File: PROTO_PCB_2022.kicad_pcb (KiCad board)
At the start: 2 copper layers, 90.8 x 50.2 mm, 35 parts, among them J1 12V_IN, J10 12V_AUX, J11 SW_START, J12 VESC_START, J2 SW_KILL_DRIVER, J3 SW_KILL_LEFT, J4 SW_KILL_RIGHT, J5 12V_ECU, J6 12V_HORN, J7 SW_BRAKE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

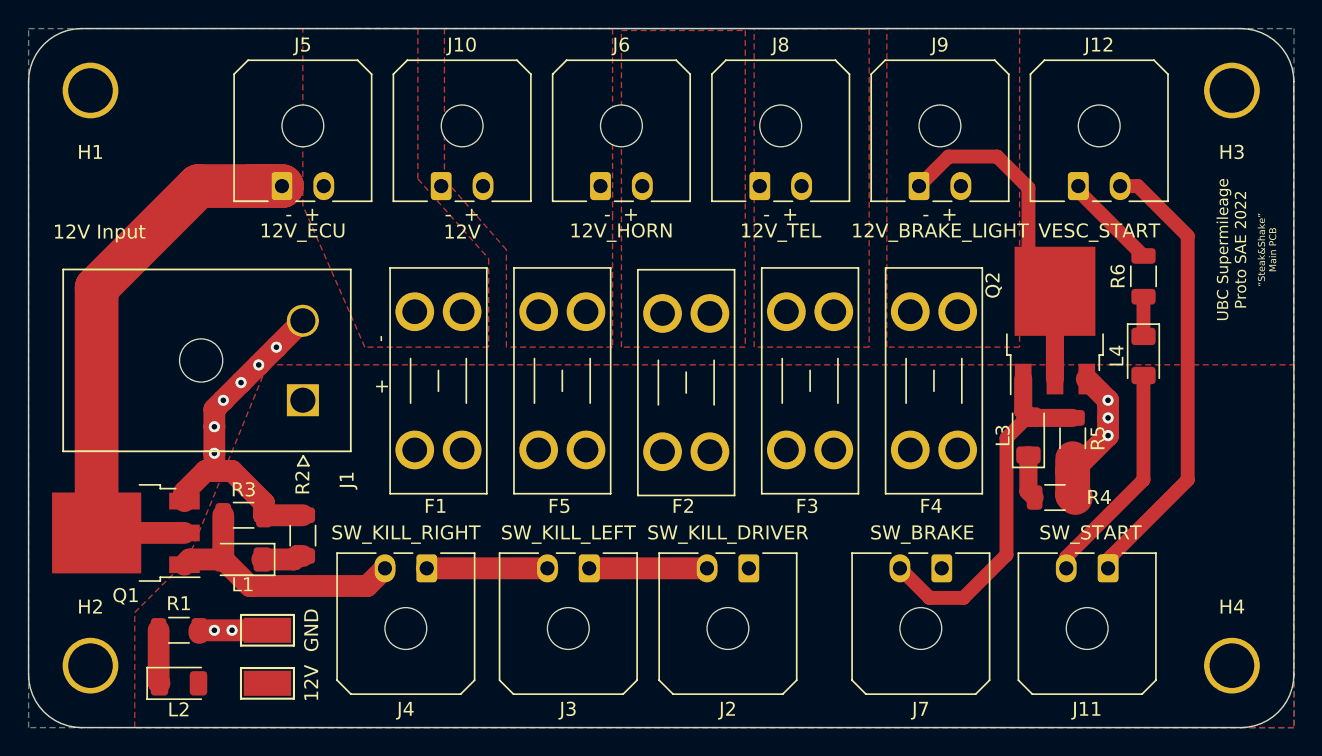
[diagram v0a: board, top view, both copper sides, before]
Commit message: added some more labels to layout and made BOM doc
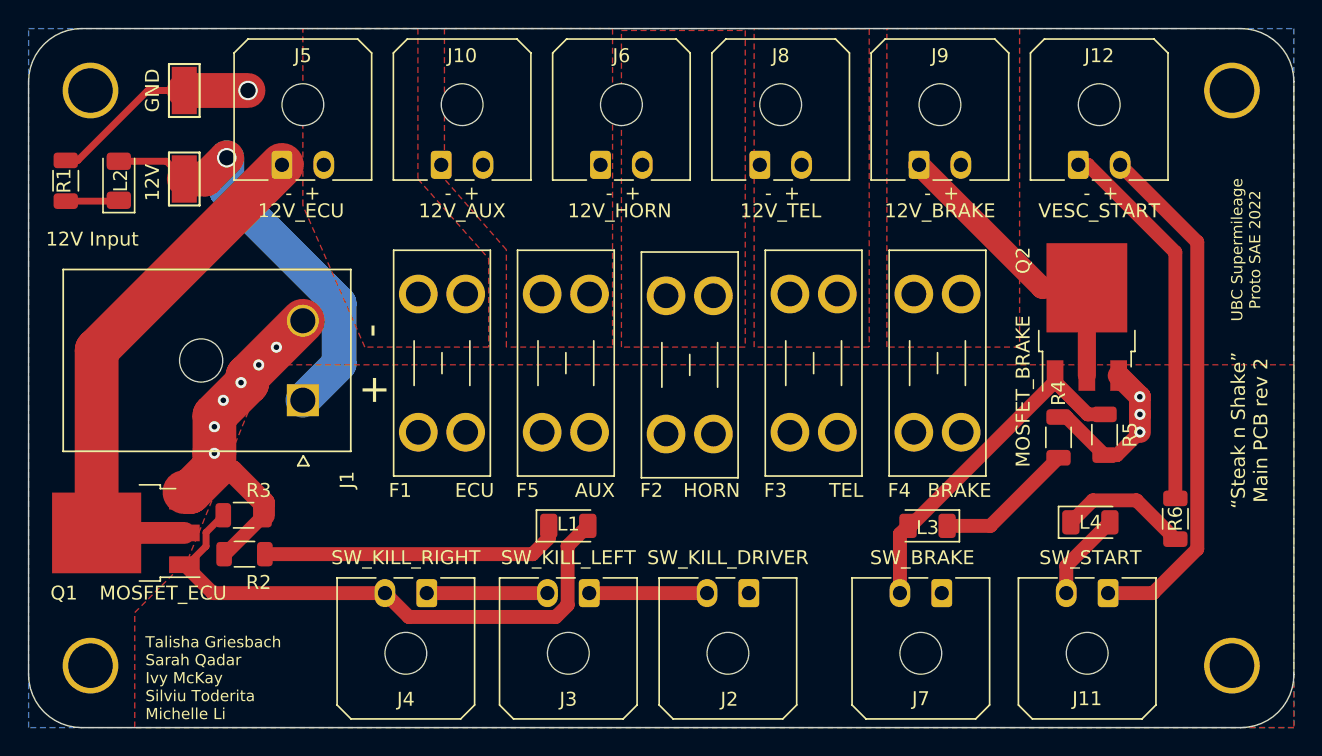
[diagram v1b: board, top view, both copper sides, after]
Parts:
- added ?: , , F.Cu at (121.4, 113.5)
- added ?: , , F.Cu at (122.9, 126.2)
- added ?: , , F.Cu at (121.7, 122.2)
- J9: value 12V_BRAKE_LIGHT -> 12V_BRAKE
- Q2: value MOSFET_BRAKE_LIGHT -> MOSFET_BRAKE
- TP1: value 12V Test -> 12V
- TP2: value GND Test -> GND
- moved TP2 39.2 mm to (52.8, 104.1), turned to 90 degrees
- moved TP1 36.7 mm to (52.8, 110.5), turned to 90 degrees
- moved L2 36.3 mm to (48.1, 110.6), turned to 90 degrees
- moved R1 33.3 mm to (44.3, 110.6), turned to 270 degrees
- moved L1 23.5 mm to (80.4, 135.4), turned to 0 degrees
- moved R6 17.5 mm to (124.0, 134.9)
- moved L4 12.5 mm to (117.9, 135.1), turned to 0 degrees
- moved L3 9.71 mm to (106.2, 135.4), turned to 180 degrees
- moved R2 4.40 mm to (57.1, 137.4), turned to 180 degrees
- moved R4 4.33 mm to (115.6, 129.0), turned to 90 degrees
- moved Q2 2.30 mm to (117.6, 120.4)
- moved R5 2.30 mm to (118.9, 128.8)
- moved J11 1.78 mm to (119.1, 140.2)
- moved J2 1.78 mm to (93.3, 140.2)
- moved J3 1.78 mm to (81.9, 140.2)
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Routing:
- net +12V: track 0.00 -> 30.7 mm, vias 0 -> 1
- net GND: track 42.5 -> 69.1 mm, vias 11 -> 10
- net Net-(J4-Pad2): track 19.0 -> 40.5 mm
- net Net-(J12-Pad1): track 6.61 -> 27.2 mm
- net Net-(L1-Pad1): track 3.02 -> 21.7 mm
- net Net-(J5-Pad1): track 56.8 -> 39.1 mm
- net Net-(J11-Pad2): track 16.1 -> 6.38 mm
- net Net-(L3-Pad1): track 3.23 -> 10.0 mm
- net Net-(L4-Pad1): track 2.85 -> 9.30 mm
- net Net-(J11-Pad1): track 33.6 -> 37.6 mm
- net Net-(J7-Pad2): track 26.5 -> 25.3 mm
- net Net-(J9-Pad1): track 24.2 -> 24.7 mm
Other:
- board text added: "12V_AUX"
- board text added: "AUX"
- board text added: "BRAKE"
- board text added: "ECU"
- board text added: "HORN"
- board text added: "TEL"
- board text added: "Talisha Griesbach Sarah Qadar Ivy McKay Silviu Toderita Michelle Li"
- board text added: "“Steak n Shake” Main PCB rev 2"
- board text removed: "12V"
- board text removed: "GND"
- board text removed: "“Steak&Shake” Main PCB"

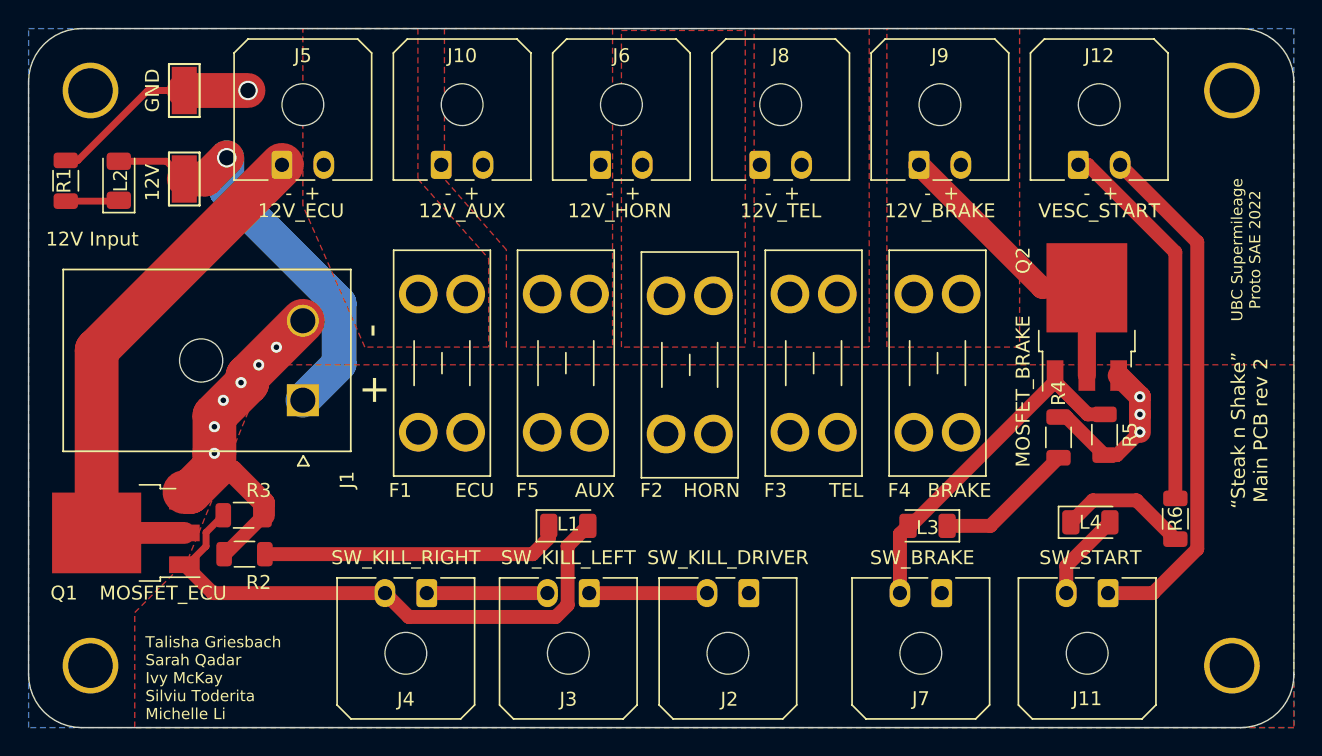
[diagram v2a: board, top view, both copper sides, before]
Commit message: Changes handlebar connector to RJ45
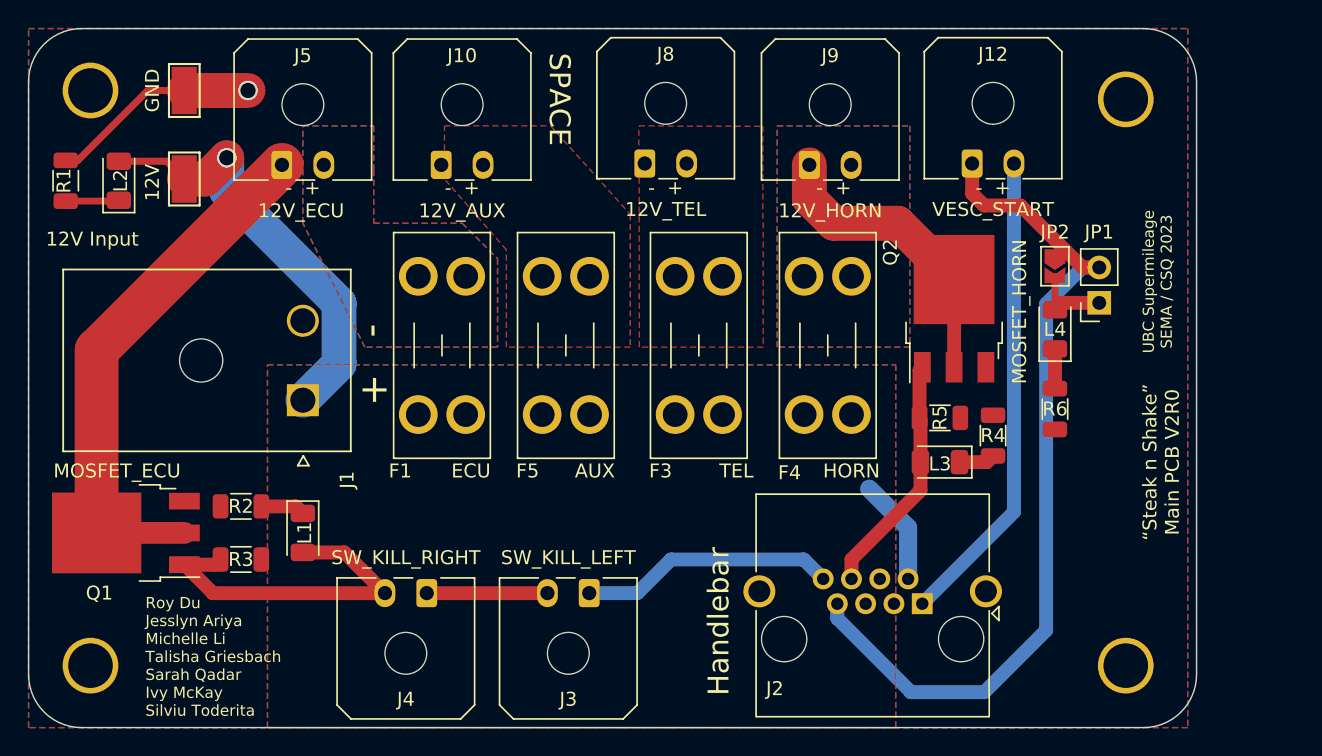
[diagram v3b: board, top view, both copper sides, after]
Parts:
- removed ? (x3): , 
- removed F2: 2A, Fuse:Fuseholder_Blade_Mini_Keystone_3568
- removed J11: SW_START, Connector_Molex:Molex_Micro-Fit_3.0_43650-0200_1x02_P3.00mm_Horizontal
- removed J6: 12V_HORN, Connector_Molex:Molex_Micro-Fit_3.0_43650-0200_1x02_P3.00mm_Horizontal
- removed J7: SW_BRAKE, Connector_Molex:Molex_Micro-Fit_3.0_43650-0200_1x02_P3.00mm_Horizontal
- added JP1: Jumper_2_Open, Connector_PinSocket_2.54mm:PinSocket_1x02_P2.54mm_Vertical, F.Cu at (118.5, 119.4)
- added JP2: SolderJumper_2_Open, Jumper:SolderJumper-2_P1.3mm_Open_TrianglePad1.0x1.5mm, F.Cu at (115.3, 116.8)
- J2: value SW_KILL_DRIVER -> Ethernet connector; footprint Connector_Molex:Molex_Micro-Fit_3.0_43650-0200_1x02_P3.00mm_Horizontal -> Connector_RJ:RJ45_Amphenol_RJHSE5380
- J9: value 12V_BRAKE -> 12V_HORN
- Q2: value MOSFET_BRAKE -> MOSFET_HORN
- moved L1 19.1 mm to (61.3, 135.9), turned to -90 degrees
- moved L4 14.1 mm to (115.3, 121.3), turned to 90 degrees
- moved J2 12.5 mm to (105.8, 141.0)
- moved R5 11.9 mm to (107.1, 127.6), turned to 0 degrees
- moved R6 11.7 mm to (115.3, 127.0)
- moved Q2 9.54 mm to (108.1, 119.8)
- moved F3 8.34 mm to (91.5, 117.5)
- moved J8 8.26 mm to (85.9, 109.4)
- moved F4 7.98 mm to (100.7, 117.5)
- moved J9 7.87 mm to (97.7, 109.5)
- moved H3 7.65 mm to (120.4, 104.8)
- moved J12 7.62 mm to (109.4, 109.4)
- moved H4 7.62 mm to (120.4, 145.4)
- moved R4 4.70 mm to (110.9, 128.9)
- moved L3 4.66 mm to (107.1, 130.8)
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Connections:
- J12 pad 1: Net-(J12-Pad1) -> /Starter_in
- J12 pad 2: Net-(J11-Pad1) -> /Starter_out
- J2 pad 1: +12V -> /Starter_out
- J2 pad 2: Net-(J2-Pad2) -> +12V
- J3 pad 1: Net-(J2-Pad2) -> /Kill
- L3 pad 2: Net-(J7-Pad2) -> /Horn
- Q2 pad 1: Net-(J7-Pad2) -> /Horn
- R5 pad 1: Net-(J7-Pad2) -> /Horn
- R6 pad 1: Net-(L4-Pad1) -> GND
- R6 pad 2: Net-(J12-Pad1) -> Net-(L4-Pad1)
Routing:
- net /Starter_in: track 0.00 -> 61.9 mm
- net GND: track 69.1 -> 15.2 mm, vias 10 -> 1
- net Net-(J11-Pad1): track 37.6 -> 0.00 mm
- net /Starter_out: track 0.00 -> 34.3 mm
- net Net-(J12-Pad1): track 27.2 -> 0.00 mm
- net Net-(J7-Pad2): track 25.3 -> 0.00 mm
- net Net-(L1-Pad1): track 21.7 -> 3.19 mm
- net /Kill: track 0.00 -> 18.4 mm
- net /Horn: track 0.00 -> 17.3 mm
- net Net-(J4-Pad2): track 40.5 -> 25.1 mm
- net Net-(J2-Pad2): track 8.45 -> 0.00 mm
- net +12V: track 30.7 -> 38.4 mm
- net Net-(L3-Pad1): track 10.0 -> 2.59 mm
- net Net-(L4-Pad1): track 9.30 -> 2.85 mm
- net Net-(J9-Pad1): track 24.7 -> 22.6 mm
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- added copper zone on B.Cu, net +12V
- added copper zone on F.Cu, net GND
- added copper zone on B.Cu, net Net-(F1-Pad1)
- added copper zone on B.Cu, net Net-(F4-Pad1)
- removed copper zone on F.Cu, net Net-(F2-Pad1)
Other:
- board size 90.8 x 50.2 mm -> 83.8 x 50.2 mm
- net class Default removed
- board text added: "Handlebar"
- board text added: "Roy Du Jesslyn Ariya Michelle Li Talisha Griesbach Sarah Qadar Ivy McKay Silviu Toderita"
- board text added: "SPACE"
- board text added: "UBC Supermileage SEMA / CSQ 2023"
- board text added: "“Steak n Shake” Main PCB V2R0"
- board text removed: "BRAKE"
- board text removed: "Talisha Griesbach Sarah Qadar Ivy McKay Silviu Toderita Michelle Li"
- board text removed: "UBC Supermileage Proto SAE 2022"
- board text removed: "“Steak n Shake” Main PCB rev 2"
